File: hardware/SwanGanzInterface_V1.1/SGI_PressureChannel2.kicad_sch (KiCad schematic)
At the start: 18 parts, among them J6 Conn_01x04_Pin, U10 OPA2350, U9 INA122D

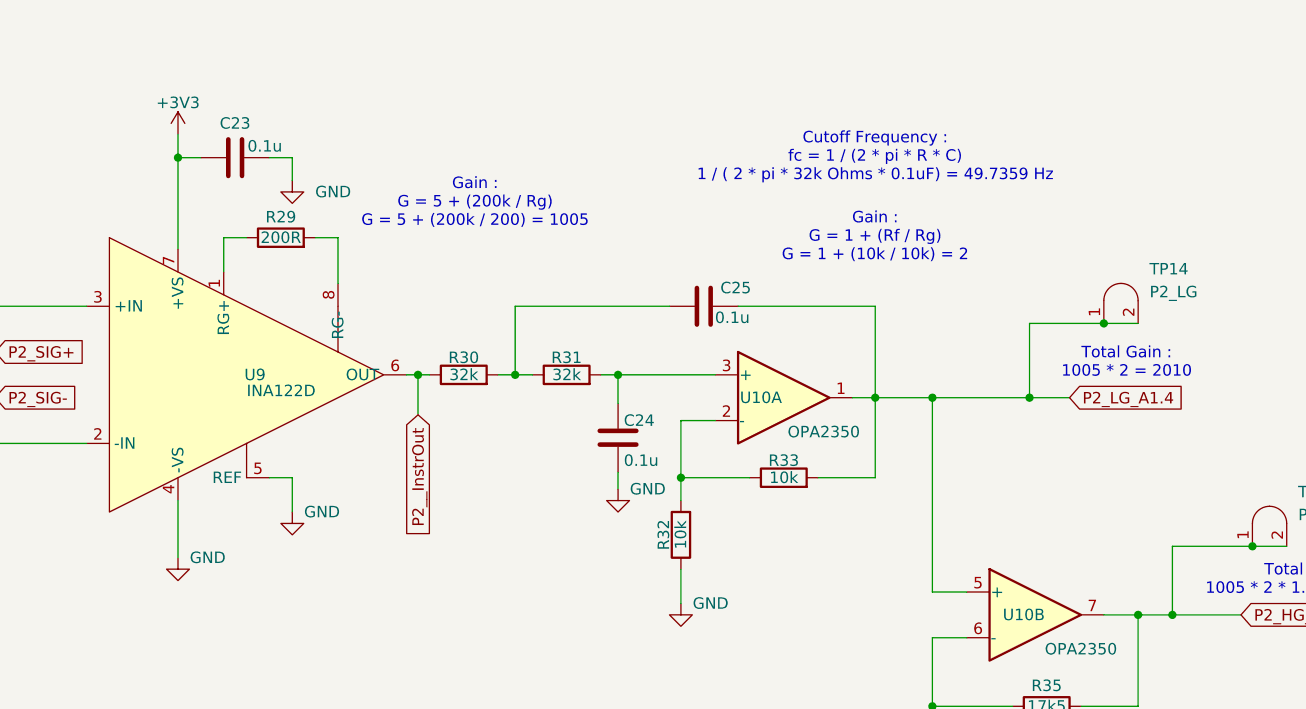
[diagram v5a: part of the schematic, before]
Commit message: Filter paramaters and assigned footprints
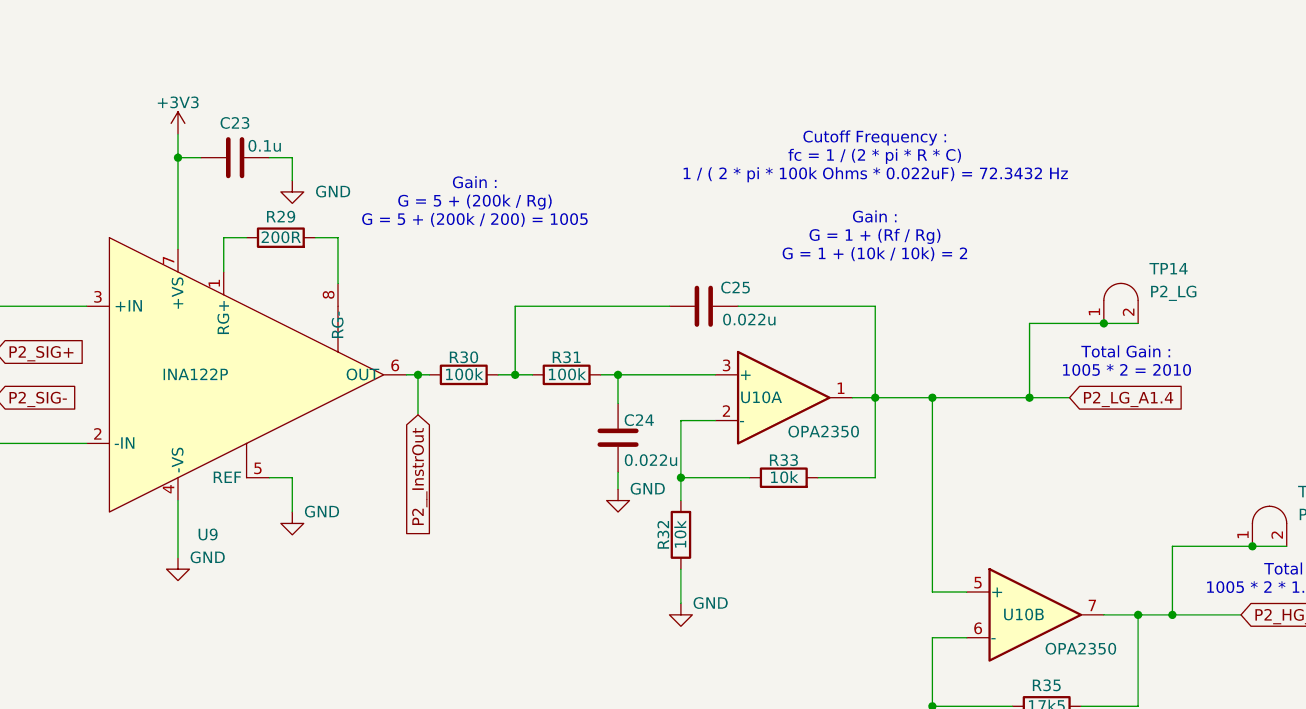
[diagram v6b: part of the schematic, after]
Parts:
- removed U9: INA122D, Package_SO:SOIC-8_5.3x5.3mm_P1.27mm, symbol SGI_SymbolLib:INA122D
- added U9: INA122P, Package_DIP:DIP-8_W7.62mm_LongPads, symbol SGI_SymbolLib:INA122P
- C24: value 0.1u -> 0.022u; footprint Capacitor_SMD:C_1206_3216Metric -> Capacitor_SMD:C_0805_2012Metric
- C25: value 0.1u -> 0.022u; footprint Capacitor_SMD:C_1206_3216Metric -> Capacitor_SMD:C_0603_1608Metric
- R30, R31: value 32k -> 100k
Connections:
- net +3V3: now also U9.7 (+VS)
- net GND: now also U9.4 (-VS), U9.5 (REF)
- net P2_SIG+: now also U9.3 (+IN)
- net P2_SIG-: now also U9.2 (-IN)
- net P2__InstrOut: now also U9.6 (OUT)
- net at R29.1: now also U9.1 (RG+)
- net at R29.2: now also U9.8 (RG-)
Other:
- note added: "Cutoff Frequency : fc = 1 / (2 * pi * R * C) 1 / ( 2 * pi * 100k Ohms * 0.022uF) = 72.3432 Hz"
- note removed: "Cutoff Frequency : fc = 1 / (2 * pi * R * C) 1 / ( 2 * pi * 32k Ohms * 0.1uF) = 49.7359 Hz"
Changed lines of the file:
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@@
 		)
 	)
-	(text "Cutoff Frequency :\nfc = 1 / (2 * pi * R * C)\n1 / ( 2 * pi * 32k Ohms * 0.1uF) = 49.7359 Hz"
+	(text "Cutoff Frequency :\nfc = 1 / (2 * pi * R * C)\n1 / ( 2 * pi * 100k Ohms * 0.022uF) = 72.3432 Hz"
 		(exclude_from_sim no)
 		(at 161.29 38.1 0)
@@
 			)
 		)
-		(property "Value" "32k"
+		(property "Value" "100k"
 			(at 115.57 62.23 90)
 			(effects
@@
 	)
 	(symbol
+		(lib_id "SGI_SymbolLib:INA122P")
+		(at 91.44 62.23 0)
+		(unit 1)
+		(exclude_from_sim no)
+		(in_bom yes)
+		(on_board yes)
+		(dnp no)
+		(property "Reference" "U9"
+			(at 85.9633 80.01 0)
+			(effects
+				(font
+					(size 1.27 1.27)
+				)
+				(justify left)
+			)
+		)
+		(property "Value" "INA122P"
+			(at 82.042 62.23 0)
+			(effects
+				(font
+					(size 1.27 1.27)
+				)
+				(justify left)
+			)
+		)
+		(property "Footprint" "Package_DIP:DIP-8_W7.62mm_LongPads"
+			(at 121.666 68.072 0)
+			(effects
+				(font
+					(size 1.27 1.27)
+				)
+				(hide yes)
+			)
+		)
+		(property "Datasheet" "kicad-embed://ina122.pdf"
+			(at 114.554 66.04 0)
+			(effects
+				(font
+					(size 1.27 1.27)
+				)
+				(hide yes)
+			)
+		)
+		(property "Description" "Instrumentation Amp"
+			(at 111.252 70.104 0)
+			(effects
+				(font
+					(size 1.27 1.27)
+				)
+				(hide yes)
+			)
+		)
+		(pin "8"
+		)
+		(pin "2"
+		)
+		(pin "6"
+		)
+		(pin "5"
+		)
+		(pin "4"
+		)
+		(pin "7"
+		)
+		(pin "3"
+		)
+		(pin "1"
+		)
+		(instances
+			(project ""
+				(path "/4e9a6e30-f660-472b-9696-bea1f34b4545/5b443651-3bea-4d19-bd25-a234ca65ad96"
+					(reference "U9")
+					(unit 1)
+				)
+			)
+		)
+	)
+	(symbol
 		(lib_id "power:GNDA")
 		(at 132.715 74.93 0)
@@
 	)
 	(symbol
-		(lib_id "SGI_SymbolLib:INA122D")
-		(at 91.44 62.23 0)
-		(unit 1)
-		(exclude_from_sim no)
-		(in_bom yes)
-		(on_board yes)
-		(dnp no)
-		(property "Reference" "U9"
-			(at 91.186 62.23 0)
-			(effects
-				(font
-					(size 1.27 1.27)
-				)
-				(justify left)
-			)
-		)
-		(property "Value" "INA122D"
-			(at 91.44 64.008 0)
-			(effects
-				(font
-					(size 1.27 1.27)
-				)
-				(justify left)
-			)
-		)
-		(property "Footprint" "Package_SO:SOIC-8_5.3x5.3mm_P1.27mm"
-			(at 121.666 68.072 0)
-			(effects
-				(font
-					(size 1.27 1.27)
-				)
-				(hide yes)
-			)
-		)
-		(property "Datasheet" "kicad-embed://ina122.pdf"
-			(at 114.554 66.04 0)
-			(effects
-				(font
-					(size 1.27 1.27)
-				)
-				(hide yes)
-			)
-		)
-		(property "Description" "Instrumentation Amp"
-			(at 111.252 70.104 0)
-			(effects
-				(font
-					(size 1.27 1.27)
-				)
-				(hide yes)
-			)
-		)
-		(pin "1"
-		)
-		(pin "8"
-		)
-		(pin "2"
-		)
-		(pin "3"
-		)
-		(pin "7"
-		)
-		(pin "4"
-		)
-		(pin "5"
-		)
-		(pin "6"
-		)
-		(instances
-			(project "SwanGanzInterface"
-				(path "/4e9a6e30-f660-472b-9696-bea1f34b4545/5b443651-3bea-4d19-bd25-a234ca65ad96"
-					(reference "U9")
-					(unit 1)
-				)
-			)
-		)
-	)
-	(symbol
 		(lib_id "Device:R")
 		(at 127 62.23 90)
@@
 			)
 		)
-		(property "Value" "32k"
+		(property "Value" "100k"
 			(at 127 62.23 90)
 			(effects
@@
 			)
 		)
-		(property "Value" "0.1u"
-			(at 145.415 55.88 90)
+		(property "Value" "0.022u"
+			(at 147.32 56.134 90)
 			(effects
 				(font
@@
 			)
 		)
-		(property "Footprint" "Capacitor_SMD:C_1206_3216Metric"
+		(property "Footprint" "Capacitor_SMD:C_0603_1608Metric"
 			(at 146.05 53.6448 0)
 			(effects
@@
 			)
 		)
-		(property "Value" "0.1u"
+		(property "Value" "0.022u"
 			(at 133.35 71.755 0)
 			(effects
@@
 			)
 		)
-		(property "Footprint" "Capacitor_SMD:C_1206_3216Metric"
+		(property "Footprint" "Capacitor_SMD:C_0805_2012Metric"
 			(at 133.6802 73.025 0)
 			(effects

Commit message: SGI v2 Layout Complete
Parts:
- renumbered C23 to C25, C24 to C26, C25 to C27, C26 to C28, J6 to J7, J7 to J8, R29 to R33, R30 to R34, R31 to R35, R32 to R36, R33 to R37, R34 to R38, R35 to R39, U9 to U10, U10 to U11
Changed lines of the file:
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@@
 		(on_board yes)
 		(dnp no)
-		(property "Reference" "#PWR066"
+		(property "Reference" "#PWR072"
 			(at 259.08 27.94 0)
 			(effects
@@
 			(project "SwanGanzInterface"
 				(path "/4e9a6e30-f660-472b-9696-bea1f34b4545/5b443651-3bea-4d19-bd25-a234ca65ad96"
-					(reference "#PWR066")
+					(reference "#PWR072")
 					(unit 1)
 				)
@@
 		(dnp no)
 		(fields_autoplaced yes)
-		(property "Reference" "U10"
+		(property "Reference" "U11"
 			(at 260.35 36.8299 0)
 			(effects
@@
 			(project "SwanGanzInterface"
 				(path "/4e9a6e30-f660-472b-9696-bea1f34b4545/5b443651-3bea-4d19-bd25-a234ca65ad96"
-					(reference "U10")
+					(reference "U11")
 					(unit 3)
 				)
@@
 		(on_board yes)
 		(dnp no)
-		(property "Reference" "#PWR057"
+		(property "Reference" "#PWR063"
 			(at 29.21 200.66 0)
 			(effects
@@
 			(project "SwanGanzInterface"
 				(path "/4e9a6e30-f660-472b-9696-bea1f34b4545/5b443651-3bea-4d19-bd25-a234ca65ad96"
-					(reference "#PWR057")
+					(reference "#PWR063")
 					(unit 1)
 				)
@@
 		(dnp no)
 		(fields_autoplaced yes)
-		(property "Reference" "J6"
+		(property "Reference" "J7"
 			(at 19.685 179.07 0)
 			(effects
@@
 			(project "SwanGanzInterface"
 				(path "/4e9a6e30-f660-472b-9696-bea1f34b4545/5b443651-3bea-4d19-bd25-a234ca65ad96"
-					(reference "J6")
+					(reference "J7")
 					(unit 1)
 				)
@@
 		(dnp no)
 		(fields_autoplaced yes)
-		(property "Reference" "J7"
+		(property "Reference" "J8"
 			(at 36.83 47.498 0)
 			(effects
@@
 			(project "SwanGanzInterface"
 				(path "/4e9a6e30-f660-472b-9696-bea1f34b4545/5b443651-3bea-4d19-bd25-a234ca65ad96"
-					(reference "J7")
+					(reference "J8")
 					(unit 1)
 				)
@@
 		(on_board yes)
 		(dnp no)
-		(property "Reference" "#PWR065"
+		(property "Reference" "#PWR071"
 			(at 167.64 118.11 0)
 			(effects
@@
 			(project "SwanGanzInterface"
 				(path "/4e9a6e30-f660-472b-9696-bea1f34b4545/5b443651-3bea-4d19-bd25-a234ca65ad96"
-					(reference "#PWR065")
+					(reference "#PWR071")
 					(unit 1)
 				)
@@
 		(on_board yes)
 		(dnp no)
-		(property "Reference" "R33"
+		(property "Reference" "R37"
 			(at 151.13 71.755 90)
 			(effects
@@
 			(project "SwanGanzInterface"
 				(path "/4e9a6e30-f660-472b-9696-bea1f34b4545/5b443651-3bea-4d19-bd25-a234ca65ad96"
-					(reference "R33")
+					(reference "R37")
 					(unit 1)
 				)
@@
 		(on_board yes)
 		(dnp no)
-		(property "Reference" "R30"
+		(property "Reference" "R34"
 			(at 115.57 60.325 90)
 			(effects
@@
 			(project "SwanGanzInterface"
 				(path "/4e9a6e30-f660-472b-9696-bea1f34b4545/5b443651-3bea-4d19-bd25-a234ca65ad96"
-					(reference "R30")
+					(reference "R34")
 					(unit 1)
 				)
@@
 		(on_board yes)
 		(dnp no)
-		(property "Reference" "U9"
+		(property "Reference" "U10"
 			(at 85.9633 80.01 0)
 			(effects
@@
 			(project ""
 				(path "/4e9a6e30-f660-472b-9696-bea1f34b4545/5b443651-3bea-4d19-bd25-a234ca65ad96"
-					(reference "U9")
+					(reference "U10")
 					(unit 1)
 				)
@@
 		(on_board yes)
 		(dnp no)
-		(property "Reference" "#PWR063"
+		(property "Reference" "#PWR069"
 			(at 132.715 81.28 0)
 			(effects
@@
 			(project "SwanGanzInterface"
 				(path "/4e9a6e30-f660-472b-9696-bea1f34b4545/5b443651-3bea-4d19-bd25-a234ca65ad96"
-					(reference "#PWR063")
+					(reference "#PWR069")
 					(unit 1)
 				)
@@
 		(on_board yes)
 		(dnp no)
-		(property "Reference" "#PWR064"
+		(property "Reference" "#PWR070"
 			(at 139.7 93.98 0)
 			(effects
@@
 			(project "SwanGanzInterface"
 				(path "/4e9a6e30-f660-472b-9696-bea1f34b4545/5b443651-3bea-4d19-bd25-a234ca65ad96"
-					(reference "#PWR064")
+					(reference "#PWR070")
 					(unit 1)
 				)
@@
 		(on_board yes)
 		(dnp no)
-		(property "Reference" "R32"
+		(property "Reference" "R36"
 			(at 137.795 80.01 90)
 			(effects
@@
 			(project "SwanGanzInterface"
 				(path "/4e9a6e30-f660-472b-9696-bea1f34b4545/5b443651-3bea-4d19-bd25-a234ca65ad96"
-					(reference "R32")
+					(reference "R36")
 					(unit 1)
 				)
@@
 		(on_board yes)
 		(dnp no)
-		(property "Reference" "R29"
+		(property "Reference" "R33"
 			(at 95.25 44.704 90)
 			(effects
@@
 			(project "SwanGanzInterface"
 				(path "/4e9a6e30-f660-472b-9696-bea1f34b4545/5b443651-3bea-4d19-bd25-a234ca65ad96"
-					(reference "R29")
+					(reference "R33")
 					(unit 1)
 				)
@@
 		(on_board yes)
 		(dnp no)
-		(property "Reference" "C26"
+		(property "Reference" "C28"
 			(at 272.415 34.29 0)
 			(effects
@@
 			(project "SwanGanzInterface"
 				(path "/4e9a6e30-f660-472b-9696-bea1f34b4545/5b443651-3bea-4d19-bd25-a234ca65ad96"
-					(reference "C26")
+					(reference "C28")
 					(unit 1)
 				)
@@
 		(dnp no)
 		(fields_autoplaced yes)
-		(property "Reference" "J7"
+		(property "Reference" "J8"
 			(at 36.83 82.296 0)
 			(effects
@@
 			(project "SwanGanzInterface"
 				(path "/4e9a6e30-f660-472b-9696-bea1f34b4545/5b443651-3bea-4d19-bd25-a234ca65ad96"
-					(reference "J7")
+					(reference "J8")
 					(unit 2)
 				)
@@
 		(on_board yes)
 		(dnp no)
-		(property "Reference" "U10"
+		(property "Reference" "U11"
 			(at 148.59 64.77 0)
 			(effects
@@
 			(project "SwanGanzInterface"
 				(path "/4e9a6e30-f660-472b-9696-bea1f34b4545/5b443651-3bea-4d19-bd25-a234ca65ad96"
-					(reference "U10")
+					(reference "U11")
 					(unit 1)
 				)
@@
 		(on_board yes)
 		(dnp no)
-		(property "Reference" "#PWR060"
+		(property "Reference" "#PWR066"
 			(at 83.82 88.9 0)
 			(effects
@@
 			(project "SwanGanzInterface"
 				(path "/4e9a6e30-f660-472b-9696-bea1f34b4545/5b443651-3bea-4d19-bd25-a234ca65ad96"
-					(reference "#PWR060")
+					(reference "#PWR066")
 					(unit 1)
 				)
@@
 		(on_board yes)
 		(dnp no)
-		(property "Reference" "R31"
+		(property "Reference" "R35"
 			(at 127 60.325 90)
 			(effects
@@
 			(project "SwanGanzInterface"
 				(path "/4e9a6e30-f660-472b-9696-bea1f34b4545/5b443651-3bea-4d19-bd25-a234ca65ad96"
-					(reference "R31")
+					(reference "R35")
 					(unit 1)
 				)
@@
 		(on_board yes)
 		(dnp no)
-		(property "Reference" "R35"
+		(property "Reference" "R39"
 			(at 180.34 96.774 90)
 			(effects
@@
 			(project "SwanGanzInterface"
 				(path "/4e9a6e30-f660-472b-9696-bea1f34b4545/5b443651-3bea-4d19-bd25-a234ca65ad96"
-					(reference "R35")
+					(reference "R39")
 					(unit 1)
 				)
@@
 		(dnp no)
 		(fields_autoplaced yes)
-		(property "Reference" "#PWR067"
+		(property "Reference" "#PWR073"
 			(at 259.08 58.42 0)
 			(effects
@@
 			(project "SwanGanzInterface"
 				(path "/4e9a6e30-f660-472b-9696-bea1f34b4545/5b443651-3bea-4d19-bd25-a234ca65ad96"
-					(reference "#PWR067")
+					(reference "#PWR073")
 					(unit 1)
 				)
@@
 		(on_board yes)
 		(dnp no)
-		(property "Reference" "#PWR059"
+		(property "Reference" "#PWR065"
 			(at 83.82 39.37 0)
 			(effects
@@
 			(project "SwanGanzInterface"
 				(path "/4e9a6e30-f660-472b-9696-bea1f34b4545/5b443651-3bea-4d19-bd25-a234ca65ad96"
-					(reference "#PWR059")
+					(reference "#PWR065")
 					(unit 1)
 				)
@@
 		(dnp no)
 		(fields_autoplaced yes)
-		(property "Reference" "#PWR061"
+		(property "Reference" "#PWR067"
 			(at 96.52 46.99 0)
 			(effects
@@
 			(project "SwanGanzInterface"
 				(path "/4e9a6e30-f660-472b-9696-bea1f34b4545/5b443651-3bea-4d19-bd25-a234ca65ad96"
-					(reference "#PWR061")
+					(reference "#PWR067")
 					(unit 1)
 				)
@@
 		(on_board yes)
 		(dnp no)
-		(property "Reference" "#PWR058"
+		(property "Reference" "#PWR064"
 			(at 49.53 78.74 0)
 			(effects
@@
 			(project "SwanGanzInterface"
 				(path "/4e9a6e30-f660-472b-9696-bea1f34b4545/5b443651-3bea-4d19-bd25-a234ca65ad96"
-					(reference "#PWR058")
+					(reference "#PWR064")
 					(unit 1)
 				)
@@
 		(on_board yes)
 		(dnp no)
-		(property "Reference" "#PWR062"
+		(property "Reference" "#PWR068"
 			(at 96.52 83.82 0)
 			(effects
@@
 			(project "SwanGanzInterface"
 				(path "/4e9a6e30-f660-472b-9696-bea1f34b4545/5b443651-3bea-4d19-bd25-a234ca65ad96"
-					(reference "#PWR062")
+					(reference "#PWR068")
 					(unit 1)
 				)
@@
 		(on_board yes)
 		(dnp no)
-		(property "Reference" "U10"
+		(property "Reference" "U11"
 			(at 177.8 88.9 0)
 			(effects
@@
 			(project "SwanGanzInterface"
 				(path "/4e9a6e30-f660-472b-9696-bea1f34b4545/5b443651-3bea-4d19-bd25-a234ca65ad96"
-					(reference "U10")
+					(reference "U11")
 					(unit 2)
 				)
@@
 		(on_board yes)
 		(dnp no)
-		(property "Reference" "C25"
+		(property "Reference" "C27"
 			(at 145.796 52.578 90)
 			(effects
@@
 			(project "SwanGanzInterface"
 				(path "/4e9a6e30-f660-472b-9696-bea1f34b4545/5b443651-3bea-4d19-bd25-a234ca65ad96"
-					(reference "C25")
+					(reference "C27")
 					(unit 1)
 				)
@@
 		(on_board yes)
 		(dnp no)
-		(property "Reference" "C24"
+		(property "Reference" "C26"
 			(at 133.35 67.31 0)
 			(effects
@@
 			(project "SwanGanzInterface"
 				(path "/4e9a6e30-f660-472b-9696-bea1f34b4545/5b443651-3bea-4d19-bd25-a234ca65ad96"
-					(reference "C24")
+					(reference "C26")
 					(unit 1)
 				)
@@
 		(on_board yes)
 		(dnp no)
-		(property "Reference" "C23"
+		(property "Reference" "C25"
 			(at 90.17 34.29 90)
 			(effects
@@
 			(project "SwanGanzInterface"
 				(path "/4e9a6e30-f660-472b-9696-bea1f34b4545/5b443651-3bea-4d19-bd25-a234ca65ad96"
-					(reference "C23")
+					(reference "C25")
 					(unit 1)
 				)
@@
 		(on_board yes)
 		(dnp no)
-		(property "Reference" "R34"
+		(property "Reference" "R38"
 			(at 165.354 106.68 90)
 			(effects
@@
 			(project "SwanGanzInterface"
 				(path "/4e9a6e30-f660-472b-9696-bea1f34b4545/5b443651-3bea-4d19-bd25-a234ca65ad96"
-					(reference "R34")
-					(unit 1)
-				)
+					(reference "R38")
+					(unit 1)
+				)
